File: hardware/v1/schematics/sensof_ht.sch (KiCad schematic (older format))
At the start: 23 parts, among them J1 Conn_01x06, J2 Conn_01x04, U1 Si4010-GT, U2 HTU21D/Si7020

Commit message: HW: Update V1 schematic to use di_kicad_library and global library
Import the di_kicad_library repository and swith the V1 schematic to use
it. Also replace symbol for HTU21D with Si7020-A20 symbol from KiCad
global library.
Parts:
- U2: symbol htu21d:HTU21D -> Sensor_Humidity:Si7020-A20
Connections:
- wire segments 84 -> 76
- no-connect marks 0 -> 1
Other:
- moved on the sheet: BT1, C10, C7, C8, C9, J2, R1, R2, U1

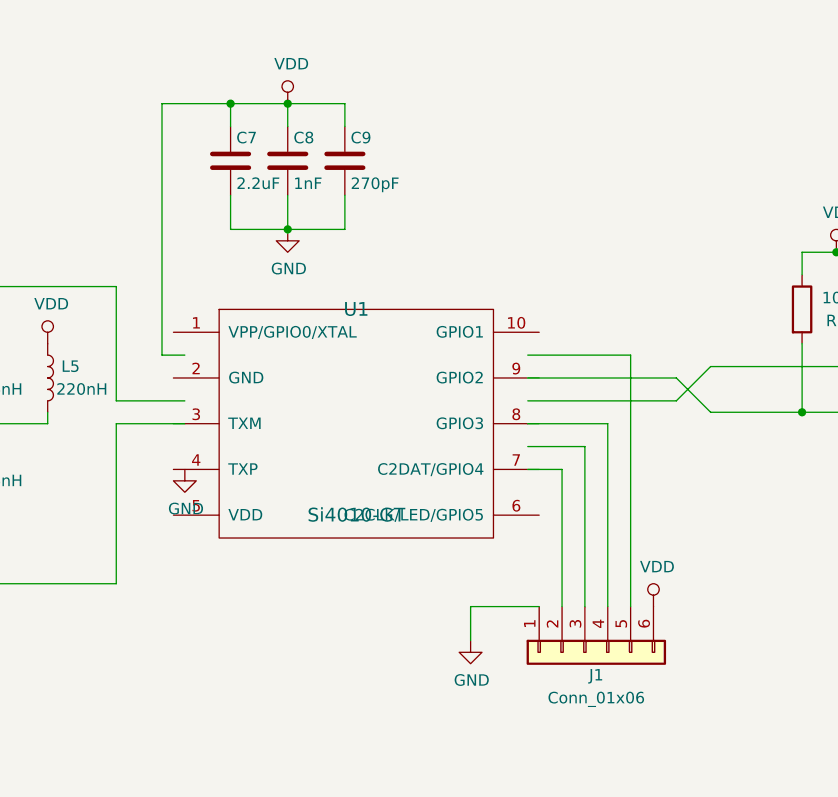
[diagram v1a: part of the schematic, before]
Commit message: Update symbol/footprints library
Some small non functional updates to shared KiCad Library.

Also updates the PCB board information with copyright etc.
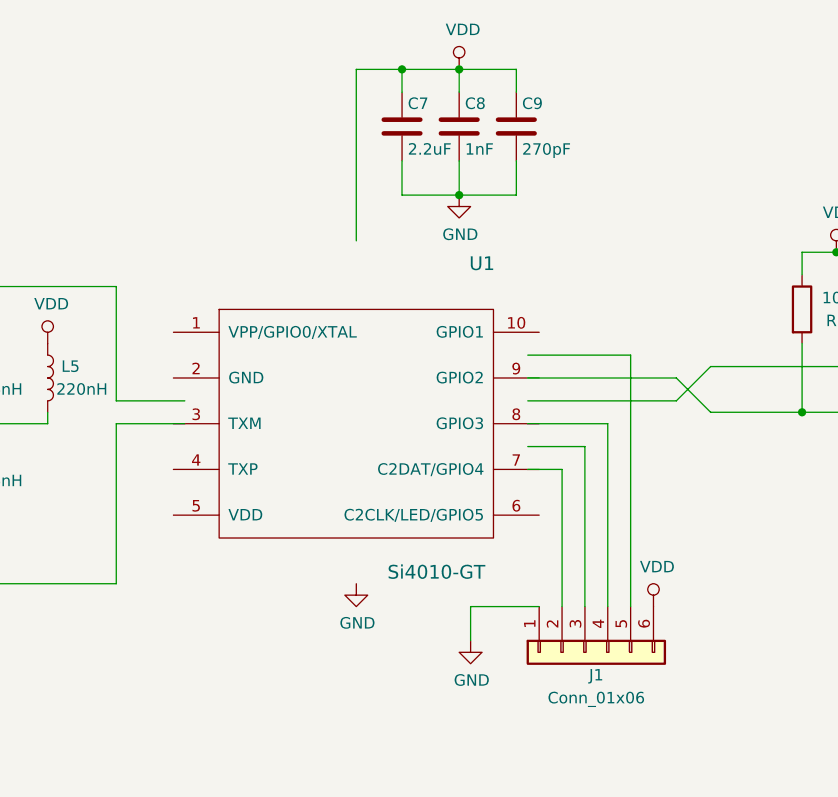
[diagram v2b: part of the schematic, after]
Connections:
- wire segments 76 -> 75
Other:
- moved on the sheet: C7, C8, C9
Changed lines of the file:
@@
 EESchema Schematic File Version 4
+LIBS:sensof_ht-cache
 EELAYER 26 0
 EELAYER END
@@
 $EndDescr
 $Comp
-L si4010:Si4010-GT U1
-U 1 1 5B3260C4
-P 5400 3550
-F 0 "U1" H 5400 4050 60  0000 C CNN
-F 1 "Si4010-GT" H 5400 3150 60  0000 C CNN
-F 2 "Housings_SSOP:MSOP-10_3x3mm_Pitch0.5mm" H 5450 3000 60  0001 C CNN
-F 3 "" H 5450 3000 60  0001 C CNN
-	1    5400 3550
-	1    0    0    -1
-$EndComp
-$Comp
 L Device:C C5
 U 1 1 5B335AB5
@@
 L Device:C C7
 U 1 1 5B33724A
-P 4850 2400
-F 0 "C7" H 4875 2500 50  0000 L CNN
-F 1 "2.2uF" H 4875 2300 50  0000 L CNN
-F 2 "Capacitors_SMD:C_0603" H 4888 2250 50  0001 C CNN
-F 3 "" H 4850 2400 50  0001 C CNN
-	1    4850 2400
+P 5600 2250
+F 0 "C7" H 5625 2350 50  0000 L CNN
+F 1 "2.2uF" H 5625 2150 50  0000 L CNN
+F 2 "Capacitors_SMD:C_0603" H 5638 2100 50  0001 C CNN
+F 3 "" H 5600 2250 50  0001 C CNN
+	1    5600 2250
 	1    0    0    -1
 $EndComp
@@
 L Device:C C8
 U 1 1 5B3372D2
-P 5100 2400
-F 0 "C8" H 5125 2500 50  0000 L CNN
-F 1 "1nF" H 5125 2300 50  0000 L CNN
-F 2 "Capacitors_SMD:C_0402" H 5138 2250 50  0001 C CNN
-F 3 "" H 5100 2400 50  0001 C CNN
-	1    5100 2400
+P 5850 2250
+F 0 "C8" H 5875 2350 50  0000 L CNN
+F 1 "1nF" H 5875 2150 50  0000 L CNN
+F 2 "Capacitors_SMD:C_0402" H 5888 2100 50  0001 C CNN
+F 3 "" H 5850 2250 50  0001 C CNN
+	1    5850 2250
 	1    0    0    -1
 $EndComp
@@
 L Device:C C9
 U 1 1 5B33736F
-P 5350 2400
-F 0 "C9" H 5375 2500 50  0000 L CNN
-F 1 "270pF" H 5375 2300 50  0000 L CNN
-F 2 "Capacitors_SMD:C_0402" H 5388 2250 50  0001 C CNN
-F 3 "" H 5350 2400 50  0001 C CNN
-	1    5350 2400
+P 6100 2250
+F 0 "C9" H 6125 2350 50  0000 L CNN
+F 1 "270pF" H 6125 2150 50  0000 L CNN
+F 2 "Capacitors_SMD:C_0402" H 6138 2100 50  0001 C CNN
+F 3 "" H 6100 2250 50  0001 C CNN
+	1    6100 2250
 	1    0    0    -1
 $EndComp
@@
 Connection ~ 3700 4250
 Wire Wire Line
-	4850 2550 4850 2700
-Wire Wire Line
-	4850 2700 5100 2700
-Wire Wire Line
-	5350 2700 5350 2550
-Connection ~ 5100 2700
-Wire Wire Line
-	5100 2700 5100 2550
-Wire Wire Line
-	5350 2150 5350 2250
-Wire Wire Line
-	4850 2150 5100 2150
-Wire Wire Line
-	5100 2150 5100 2250
-Connection ~ 5100 2150
+	5600 2400 5600 2550
+Wire Wire Line
+	5600 2550 5850 2550
+Wire Wire Line
+	6100 2550 6100 2400
+Connection ~ 5850 2550
+Wire Wire Line
+	5850 2550 5850 2400
+Wire Wire Line
+	6100 2000 6100 2100
+Wire Wire Line
+	5600 2000 5850 2000
+Wire Wire Line
+	5850 2000 5850 2100
+Connection ~ 5850 2000
 Wire Wire Line
 	7350 3200 7350 3500
@@
 	3700 4250 4350 4250
 Wire Wire Line
-	5100 2700 5350 2700
-Wire Wire Line
-	4850 2150 4850 2250
-Wire Wire Line
-	5100 2150 5350 2150
+	5850 2550 6100 2550
+Wire Wire Line
+	5600 2000 5600 2100
+Wire Wire Line
+	5850 2000 6100 2000
 Wire Wire Line
 	7350 3500 7900 3500
@@
 L power:GND #PWR0101
 U 1 1 5B82D11A
-P 5100 2700
-F 0 "#PWR0101" H 5100 2450 50  0001 C CNN
-F 1 "GND" H 5105 2527 50  0000 C CNN
-F 2 "" H 5100 2700 50  0001 C CNN
-F 3 "" H 5100 2700 50  0001 C CNN
-	1    5100 2700
+P 5850 2550
+F 0 "#PWR0101" H 5850 2300 50  0001 C CNN
+F 1 "GND" H 5855 2377 50  0000 C CNN
+F 2 "" H 5850 2550 50  0001 C CNN
+F 3 "" H 5850 2550 50  0001 C CNN
+	1    5850 2550
 	1    0    0    -1
 $EndComp
@@
 L power:GND #PWR0102
 U 1 1 5B82D15A
-P 4650 3750
-F 0 "#PWR0102" H 4650 3500 50  0001 C CNN
-F 1 "GND" H 4655 3577 50  0000 C CNN
-F 2 "" H 4650 3750 50  0001 C CNN
-F 3 "" H 4650 3750 50  0001 C CNN
-	1    4650 3750
+P 5400 4250
+F 0 "#PWR0102" H 5400 4000 50  0001 C CNN
+F 1 "GND" H 5405 4077 50  0000 C CNN
+F 2 "" H 5400 4250 50  0001 C CNN
+F 3 "" H 5400 4250 50  0001 C CNN
+	1    5400 4250
 	1    0    0    -1
 $EndComp
@@
 L power:VDD #PWR0108
 U 1 1 5B82D41A
-P 5100 2150
-F 0 "#PWR0108" H 5100 2000 50  0001 C CNN
-F 1 "VDD" H 5117 2323 50  0000 C CNN
-F 2 "" H 5100 2150 50  0001 C CNN
-F 3 "" H 5100 2150 50  0001 C CNN
-	1    5100 2150
+P 5850 2000
+F 0 "#PWR0108" H 5850 1850 50  0001 C CNN
+F 1 "VDD" H 5867 2173 50  0000 C CNN
+F 2 "" H 5850 2000 50  0001 C CNN
+F 3 "" H 5850 2000 50  0001 C CNN
+	1    5850 2000
 	1    0    0    -1
 $EndComp
@@
 	6600 3250 6600 4350
 Wire Wire Line
-	4850 2150 4550 2150
-Wire Wire Line
-	4550 2150 4550 3250
-Wire Wire Line
-	4550 3250 4650 3250
-Connection ~ 4850 2150
+	5600 2000 5400 2000
+Connection ~ 5600 2000
 Wire Wire Line
 	6150 3750 6300 3750
@@
 	6500 3550 6500 4350
 Wire Wire Line
-	6150 3350 6800 3350
-Wire Wire Line
 	8450 4650 8450 4800
 Wire Wire Line
@@
 Wire Wire Line
 	6950 3300 6800 3450
-Wire Wire Line
-	6800 3450 6150 3450
 Wire Wire Line
 	6950 3300 7650 3300
@@
 Connection ~ 8900 2550
 $Comp
-L power:GND #PWR?
+L power:GND #PWR0118
 U 1 1 5B8896B0
 P 8600 3700
-F 0 "#PWR?" H 8600 3450 50  0001 C CNN
+F 0 "#PWR0118" H 8600 3450 50  0001 C CNN
 F 1 "GND" H 8605 3527 50  0000 C CNN
 F 2 "" H 8600 3700 50  0001 C CNN
@@
 $EndComp
 NoConn ~ 8800 3700
+$Comp
+L si4010:Si4010-GT U1
+U 1 1 5B3260C4
+P 5400 3550
+F 0 "U1" H 5950 4250 60  0000 C CNN
+F 1 "Si4010-GT" H 5750 2900 60  0000 C CNN
+F 2 "Housings_SSOP:MSOP-10_3x3mm_Pitch0.5mm" H 5450 3000 60  0001 C CNN
+F 3 "" H 5450 3000 60  0001 C CNN
+	1    5400 3550
+	1    0    0    -1
+$EndComp
+Wire Wire Line
+	6150 3350 6800 3350
+Wire Wire Line
+	6150 3450 6800 3450
+Wire Wire Line
+	5400 2750 5400 2000
 $EndSCHEMATC

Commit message: HW: Added BOM suggestions to schematic for V1 hardware
Add Manufacturer, mfr. no, mouser no fields to schematic.
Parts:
- C1: Manufacturer (none) -> Murata; Mfr. No (none) -> GRM1555C1H271JA01J; Mouser No (none) -> 81-GRM1555C1H271JA1J; Note (none) -> ±5%; C0G (based on 4010-DKPB434-BM_BOM.xls)
- C10: Manufacturer (none) -> Wurth Electronics; Mfr. No (none) -> 885012105016; Mouser No (none) -> 710-885012105016
- C2, C4: Manufacturer (none) -> Murata; Mfr. No (none) -> GRM1555C1E6R8BA01D; Mouser No (none) -> 81-GRM1555C1E6R8BA1D; Note (none) -> ±5%; C0G (based on 4010-DKPB434-BM_BOM.xls)
- C3: Manufacturer (none) -> Murata; Mfr. No (none) -> GRM1555C1E4R3BA01D; Mouser No (none) -> 81-GRM1555C1E4R3BA1D; Note (none) -> ±5%; C0G (based on 4010-DKPB434-BM_BOM.xls)
- C5: Manufacturer (none) -> Murata; Mfr. No (none) -> GRM1555C1H2R7BA01D; Mouser No (none) -> 81-GRM1555C1H2R7BA1D; Note (none) -> ±5%; C0G (based on 4010-DKPB434-BM_BOM.xls)
- C6: Manufacturer (none) -> Murata; Mfr. No (none) -> GRM1555C1H1R8WA01D; Mouser No (none) -> 81-GRM1555C1H1R8WA1D; Note (none) -> ±5%; C0G (based on 4010-DKPB434-BM_BOM.xls)
- C7: Manufacturer (none) -> Wurth Electronics; Mfr. No (none) -> 885012106018; Mouser No (none) -> 710-885012106018
- C8: Manufacturer (none) -> Murata; Mfr. No (none) -> GRM1555C1H102JA01D; Mouser No (none) -> 81-GRM1555C1H102JA1D
- C9: Manufacturer (none) -> Murata; Mfr. No (none) -> GRM1555C1H271JA01J; Mouser No (none) -> 81-GRM1555C1H271JA1J
- J1: Manufacturer (none) -> SparkFun; Mfr. No (none) -> PRT-10210; Mouser No (none) -> 474-PRT-10210
- L1: Manufacturer (none) -> Murata; Mfr. No (none) -> LQW15AN18NJ80D; Mouser No (none) -> 81-LQW15AN18NJ80D; Note (none) -> See sensof_ht-BOM.ods:‘Inductor Selection’ tab
- L2: Manufacturer (none) -> Murata; Mfr. No (none) -> LQW15AN56NJ80D; Mouser No (none) -> 81-LQW15AN56NJ80D; Note (none) -> See sensof_ht-BOM.ods:‘Inductor Selection’ tab
- L3, L4: Manufacturer (none) -> Murata; Mfr. No (none) -> LQW15AN16NJ80D; Mouser No (none) -> 81-LQW15AN16NJ80D; Note (none) -> See sensof_ht-BOM.ods:‘Inductor Selection’ tab
- L5: Manufacturer (none) -> Murata; Mfr. No (none) -> LQW15CNR22J10D; Mouser No (none) -> 81-LQW15CNR22J10D; Note (none) -> See sensof_ht-BOM.ods:‘Inductor Selection’ tab
- R1, R2: Manufacturer (none) -> Vishay; Mfr. No (none) -> CRCW040210K0FKEDC; Mouser No (none) -> 71-CRCW040210K0FKEDC
- U1: Manufacturer (none) -> Silicon Labs; Mfr. No (none) -> SI4010-C2-GT; Mouser No (none) -> 634-SI4010-C2-GT
- U2: Manufacturer (none) -> Silicon Labs; Mfr. No (none) -> SI7020-A20-GM1; Mouser No (none) -> 634-SI7020-A20-GM1
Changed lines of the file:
@@
 EESchema Schematic File Version 4
-LIBS:sensof_ht-cache
 EELAYER 26 0
 EELAYER END
@@
 F 2 "silabs_0402:C_0402" H 3388 3550 50  0001 C CNN
 F 3 "" H 3350 3700 50  0001 C CNN
+F 4 "Murata" H 0   0   50  0001 C CNN "Manufacturer"
+F 5 "GRM1555C1H2R7BA01D" H 0   0   50  0001 C CNN "Mfr. No"
+F 6 "81-GRM1555C1H2R7BA1D" H 0   0   50  0001 C CNN "Mouser No"
+F 7 "±5%; C0G (based on 4010-DKPB434-BM_BOM.xls)" H 0   0   50  0001 C CNN "Note"
 	1    3350 3700
 	-1   0    0    1
@@
 F 2 "silabs_0402:C_0402" H 2538 2800 50  0001 C CNN
 F 3 "" H 2500 2950 50  0001 C CNN
+F 4 "Murata" H 0   0   50  0001 C CNN "Manufacturer"
+F 5 "GRM1555C1E4R3BA01D" H 0   0   50  0001 C CNN "Mfr. No"
+F 6 "81-GRM1555C1E4R3BA1D" H 0   0   50  0001 C CNN "Mouser No"
+F 7 "±5%; C0G (based on 4010-DKPB434-BM_BOM.xls)" H 0   0   50  0001 C CNN "Note"
 	1    2500 2950
 	0    1    1    0
@@
 F 2 "silabs_0402:C_0402" H 2188 4350 50  0001 C CNN
 F 3 "" H 2150 4500 50  0001 C CNN
+F 4 "Murata" H 0   0   50  0001 C CNN "Manufacturer"
+F 5 "GRM1555C1E6R8BA01D" H 0   0   50  0001 C CNN "Mfr. No"
+F 6 "81-GRM1555C1E6R8BA1D" H 0   0   50  0001 C CNN "Mouser No"
+F 7 "±5%; C0G (based on 4010-DKPB434-BM_BOM.xls)" H 0   0   50  0001 C CNN "Note"
 	1    2150 4500
 	1    0    0    -1
@@
 F 2 "silabs_0402:C_0402" H 2788 4350 50  0001 C CNN
 F 3 "" H 2750 4500 50  0001 C CNN
+F 4 "Murata" H 0   0   50  0001 C CNN "Manufacturer"
+F 5 "GRM1555C1E6R8BA01D" H 0   0   50  0001 C CNN "Mfr. No"
+F 6 "81-GRM1555C1E6R8BA1D" H 0   0   50  0001 C CNN "Mouser No"
+F 7 "±5%; C0G (based on 4010-DKPB434-BM_BOM.xls)" H 0   0   50  0001 C CNN "Note"
 	1    2750 4500
 	1    0    0    -1
@@
 F 2 "silabs_0402:C_0402" H 1888 4100 50  0001 C CNN
 F 3 "" H 1850 4250 50  0001 C CNN
+F 4 "Murata" V 1850 4250 50  0001 C CNN "Manufacturer"
+F 5 "GRM1555C1H271JA01J" V 1850 4250 50  0001 C CNN "Mfr. No"
+F 6 "81-GRM1555C1H271JA1J" V 1850 4250 50  0001 C CNN "Mouser No"
+F 7 "±5%; C0G (based on 4010-DKPB434-BM_BOM.xls)" V 1850 4250 50  0001 C CNN "Note"
 	1    1850 4250
 	0    1    1    0
@@
 F 2 "silabs_0402:C_0402" H 3438 4100 50  0001 C CNN
 F 3 "" H 3400 4250 50  0001 C CNN
+F 4 "Murata" H 0   0   50  0001 C CNN "Manufacturer"
+F 5 "GRM1555C1H1R8WA01D" H 0   0   50  0001 C CNN "Mfr. No"
+F 6 "81-GRM1555C1H1R8WA1D" H 0   0   50  0001 C CNN "Mouser No"
+F 7 "±5%; C0G (based on 4010-DKPB434-BM_BOM.xls)" H 0   0   50  0001 C CNN "Note"
 	1    3400 4250
 	0    1    1    0
@@
 F 2 "silabs_0402:C_0402" H 3700 3750 50  0001 C CNN
 F 3 "" H 3700 3750 50  0001 C CNN
+F 4 "Murata" H 0   0   50  0001 C CNN "Manufacturer"
+F 5 "LQW15AN16NJ80D" H 0   0   50  0001 C CNN "Mfr. No"
+F 6 "81-LQW15AN16NJ80D" H 0   0   50  0001 C CNN "Mouser No"
+F 7 "See sensof_ht-BOM.ods:‘Inductor Selection’ tab" H 0   0   50  0001 C CNN "Note"
 	1    3700 3750
 	1    0    0    -1
@@
 F 2 "silabs_0402:C_0402" H 3700 3350 50  0001 C CNN
 F 3 "" H 3700 3350 50  0001 C CNN
+F 4 "Murata" H 0   0   50  0001 C CNN "Manufacturer"
+F 5 "LQW15AN16NJ80D" H 0   0   50  0001 C CNN "Mfr. No"
+F 6 "81-LQW15AN16NJ80D" H 0   0   50  0001 C CNN "Mouser No"
+F 7 "See sensof_ht-BOM.ods:‘Inductor Selection’ tab" H 0   0   50  0001 C CNN "Note"
 	1    3700 3350
 	1    0    0    -1
@@
 F 2 "silabs_0402:C_0402" H 4050 3350 50  0001 C CNN
 F 3 "" H 4050 3350 50  0001 C CNN
+F 4 "Murata" H 0   0   50  0001 C CNN "Manufacturer"
+F 5 "LQW15CNR22J10D" H 0   0   50  0001 C CNN "Mfr. No"
+F 6 "81-LQW15CNR22J10D" H 0   0   50  0001 C CNN "Mouser No"
+F 7 "See sensof_ht-BOM.ods:‘Inductor Selection’ tab" H 0   0   50  0001 C CNN "Note"
 	1    4050 3350
 	1    0    0    -1
@@
 F 2 "silabs_0402:C_0402" H 2900 3550 50  0001 C CNN
 F 3 "" H 2900 3550 50  0001 C CNN
+F 4 "Murata" H 0   0   50  0001 C CNN "Manufacturer"
+F 5 "LQW15AN56NJ80D" H 0   0   50  0001 C CNN "Mfr. No"
+F 6 "81-LQW15AN56NJ80D" H 0   0   50  0001 C CNN "Mouser No"
+F 7 "See sensof_ht-BOM.ods:‘Inductor Selection’ tab" H 0   0   50  0001 C CNN "Note"
 	1    2900 3550
 	1    0    0    -1
@@
 F 2 "silabs_0402:C_0402" H 2450 4250 50  0001 C CNN
 F 3 "" H 2450 4250 50  0001 C CNN
+F 4 "Murata" H 0   0   50  0001 C CNN "Manufacturer"
+F 5 "LQW15AN18NJ80D" H 0   0   50  0001 C CNN "Mfr. No"
+F 6 "81-LQW15AN18NJ80D" H 0   0   50  0001 C CNN "Mouser No"
+F 7 "See sensof_ht-BOM.ods:‘Inductor Selection’ tab" H 0   0   50  0001 C CNN "Note"
 	1    2450 4250
 	0    1    1    0
@@
 F 2 "Capacitors_SMD:C_0603" H 5638 2100 50  0001 C CNN
 F 3 "" H 5600 2250 50  0001 C CNN
+F 4 "Wurth Electronics" H 0   0   50  0001 C CNN "Manufacturer"
+F 5 "885012106018" H 0   0   50  0001 C CNN "Mfr. No"
+F 6 "710-885012106018" H 0   0   50  0001 C CNN "Mouser No"
 	1    5600 2250
 	1    0    0    -1
@@
 F 2 "Capacitors_SMD:C_0402" H 5888 2100 50  0001 C CNN
 F 3 "" H 5850 2250 50  0001 C CNN
+F 4 "Murata" H 0   0   50  0001 C CNN "Manufacturer"
+F 5 "GRM1555C1H102JA01D" H 0   0   50  0001 C CNN "Mfr. No"
+F 6 "81-GRM1555C1H102JA1D" H 0   0   50  0001 C CNN "Mouser No"
 	1    5850 2250
 	1    0    0    -1
@@
 F 2 "Capacitors_SMD:C_0402" H 6138 2100 50  0001 C CNN
 F 3 "" H 6100 2250 50  0001 C CNN
+F 4 "Murata" H 0   0   50  0001 C CNN "Manufacturer"
+F 5 "GRM1555C1H271JA01J" H 0   0   50  0001 C CNN "Mfr. No"
+F 6 "81-GRM1555C1H271JA1J" H 0   0   50  0001 C CNN "Mouser No"
 	1    6100 2250
 	1    0    0    -1
@@
 F 2 "Housings_DFN_QFN:DFN-6-1EP_3x3mm_Pitch0.95mm" H 8700 3400 60  0001 C CNN
 F 3 "" H 8700 3400 60  0001 C CNN
+F 4 "Silicon Labs" H 0   0   50  0001 C CNN "Manufacturer"
+F 5 "SI7020-A20-GM1" H 0   0   50  0001 C CNN "Mfr. No"
+F 6 "634-SI7020-A20-GM1" H 0   0   50  0001 C CNN "Mouser No"
 	1    8700 3400
 	1    0    0    -1
@@
 F 2 "Resistors_SMD:R_0402" V 7580 3050 50  0001 C CNN
 F 3 "" H 7650 3050 50  0001 C CNN
+F 4 "Vishay" H 0   0   50  0001 C CNN "Manufacturer"
+F 5 "CRCW040210K0FKEDC" H 0   0   50  0001 C CNN "Mfr. No"
+F 6 "71-CRCW040210K0FKEDC" H 0   0   50  0001 C CNN "Mouser No"
 	1    7650 3050
 	1    0    0    -1
@@
 F 2 "Resistors_SMD:R_0402" V 7280 3050 50  0001 C CNN
 F 3 "" H 7350 3050 50  0001 C CNN
+F 4 "Vishay" H 0   0   50  0001 C CNN "Manufacturer"
+F 5 "CRCW040210K0FKEDC" H 0   0   50  0001 C CNN "Mfr. No"
+F 6 "71-CRCW040210K0FKEDC" H 0   0   50  0001 C CNN "Mouser No"
 	1    7350 3050
 	1    0    0    -1
@@
 F 2 "Connectors_JST:JST_SH_SM06B-SRSS-TB_06x1.00mm_Angled" H 6400 4550 50  0001 C CNN
 F 3 "" H 6400 4550 50  0001 C CNN
+F 4 "SparkFun" H 0   0   50  0001 C CNN "Manufacturer"
+F 5 "PRT-10210" H 0   0   50  0001 C CNN "Mfr. No"
+F 6 "474-PRT-10210" H 0   0   50  0001 C CNN "Mouser No"
 	1    6400 4550
 	0    -1   1    0
@@
 F 2 "Capacitors_SMD:C_0402" H 8938 2550 50  0001 C CNN
 F 3 "" H 8900 2700 50  0001 C CNN
+F 4 "Wurth Electronics" H 0   0   50  0001 C CNN "Manufacturer"
+F 5 "885012105016" H 0   0   50  0001 C CNN "Mfr. No"
+F 6 "710-885012105016" H 0   0   50  0001 C CNN "Mouser No"
 	1    8900 2700
 	1    0    0    -1
@@
 F 2 "Housings_SSOP:MSOP-10_3x3mm_Pitch0.5mm" H 5450 3000 60  0001 C CNN
 F 3 "" H 5450 3000 60  0001 C CNN
+F 4 "Silicon Labs" H 0   0   50  0001 C CNN "Manufacturer"
+F 5 "SI4010-C2-GT" H 0   0   50  0001 C CNN "Mfr. No"
+F 6 "634-SI4010-C2-GT" H 0   0   50  0001 C CNN "Mouser No"
 	1    5400 3550
 	1    0    0    -1
